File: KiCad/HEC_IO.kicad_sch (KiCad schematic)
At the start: 23 parts, among them SW1 SW_DIP_x04, U12 74LS04, U17 74LS20, U22 74LS02, U30 74LS74, U31 74LS32, U32 LM79M05_TO220, U33 74LS20, U34 74LS393, U35 74LS08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

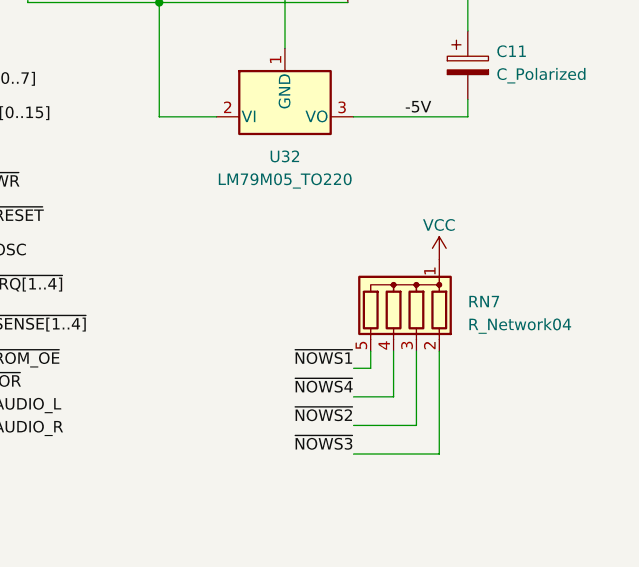
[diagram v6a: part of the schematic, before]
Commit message: Change resistor network, add revision number
Changed most of the resistor network footprints so that they would accept both 9 pin and 5 pin resistor networks (since I bought 50 of those 5 pin ones!). Power routing optimizations. Added a revision number to the silkscreen to distinguish the board
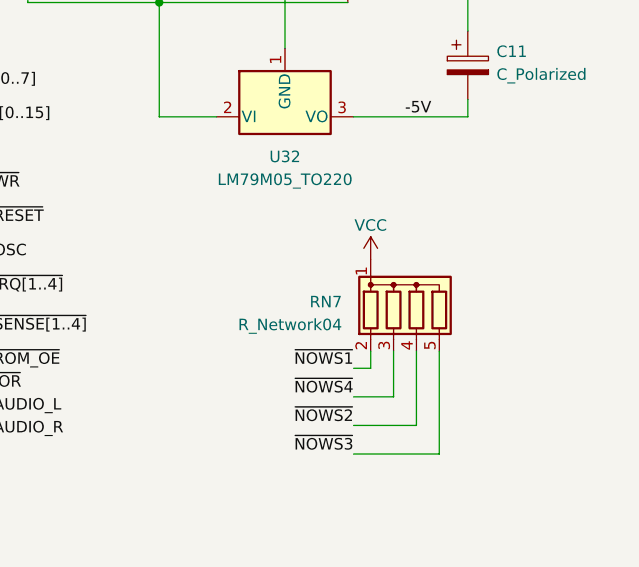
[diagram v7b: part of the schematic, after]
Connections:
- net ~{NOWS1}: now also RN7.2 (R1); no longer RN7.5 (R4)
- net ~{NOWS2}: now also RN7.4 (R3); no longer RN7.3 (R2)
- net ~{NOWS3}: now also RN7.5 (R4); no longer RN7.2 (R1)
- net ~{NOWS4}: now also RN7.3 (R2); no longer RN7.4 (R3)
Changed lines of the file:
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@@
     )
   )
-  (symbol (lib_id "Device:R_Network04") (at 260.35 66.04 0) (mirror y) (unit 1)
-    (in_bom yes) (on_board yes) (dnp no) (fields_autoplaced)
-    (property "Reference" "RN7" (at 268.605 65.659 0)
+  (symbol (lib_id "Device:R_Network04") (at 262.89 66.04 0) (unit 1)
+    (in_bom yes) (on_board yes) (dnp no)
+    (property "Reference" "RN7" (at 254.635 65.659 0)
       (effects (font (size 1.27 1.27)) (justify right))
     )
-    (property "Value" "R_Network04" (at 268.605 68.199 0)
+    (property "Value" "R_Network04" (at 254.635 68.199 0)
       (effects (font (size 1.27 1.27)) (justify right))
     )
-    (property "Footprint" "Resistor_THT:R_Array_SIP5" (at 253.365 66.04 90)
-      (effects (font (size 1.27 1.27)) hide)
-    )
-    (property "Datasheet" "http://www.vishay.com/docs/31509/csc.pdf" (at 260.35 66.04 0)
+    (property "Footprint" "Resistor_THT:R_Array_SIP5" (at 269.875 66.04 90)
+      (effects (font (size 1.27 1.27)) hide)
+    )
+    (property "Datasheet" "http://www.vishay.com/docs/31509/csc.pdf" (at 262.89 66.04 0)
       (effects (font (size 1.27 1.27)) hide)
     )
@@
     )
   )
-  (symbol (lib_id "power:VCC") (at 265.43 60.96 0) (unit 1)
-    (in_bom yes) (on_board yes) (dnp no) (fields_autoplaced)
-    (property "Reference" "#PWR0130" (at 265.43 64.77 0)
-      (effects (font (size 1.27 1.27)) hide)
-    )
-    (property "Value" "VCC" (at 265.43 57.15 0)
-      (effects (font (size 1.27 1.27)))
-    )
-    (property "Footprint" "" (at 265.43 60.96 0)
-      (effects (font (size 1.27 1.27)) hide)
-    )
-    (property "Datasheet" "" (at 265.43 60.96 0)
-      (effects (font (size 1.27 1.27)) hide)
-    )
+  (symbol (lib_id "power:VCC") (at 257.81 60.96 0) (unit 1)
+    (in_bom yes) (on_board yes) (dnp no) (fields_autoplaced)
+    (property "Reference" "#PWR0130" (at 257.81 64.77 0)
+      (effects (font (size 1.27 1.27)) hide)
+    )
+    (property "Value" "VCC" (at 257.81 57.15 0)
+      (effects (font (size 1.27 1.27)))
+    )
+    (property "Footprint" "" (at 257.81 60.96 0)
+      (effects (font (size 1.27 1.27)) hide)
+    )
+    (property "Datasheet" "" (at 257.81 60.96 0)
+      (effects (font (size 1.27 1.27)) hide)
+    )

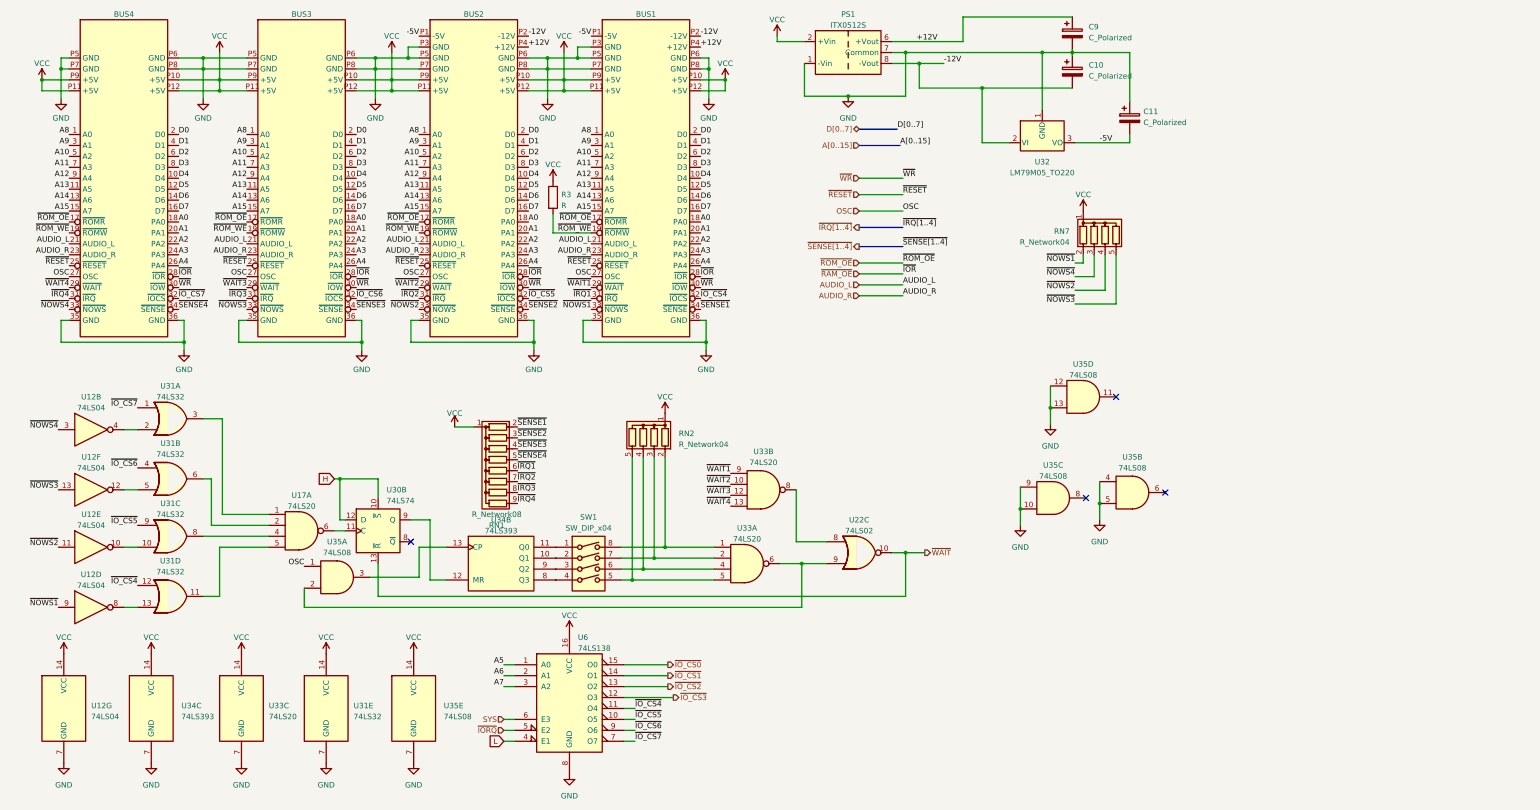
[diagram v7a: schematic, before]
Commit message: Add I2C bus
Change audio pins on the bus to carry I2C signal. This can be used for configuring onboard devices such as RGB to HDMI converters, sound mixers, GPIOs, etc.
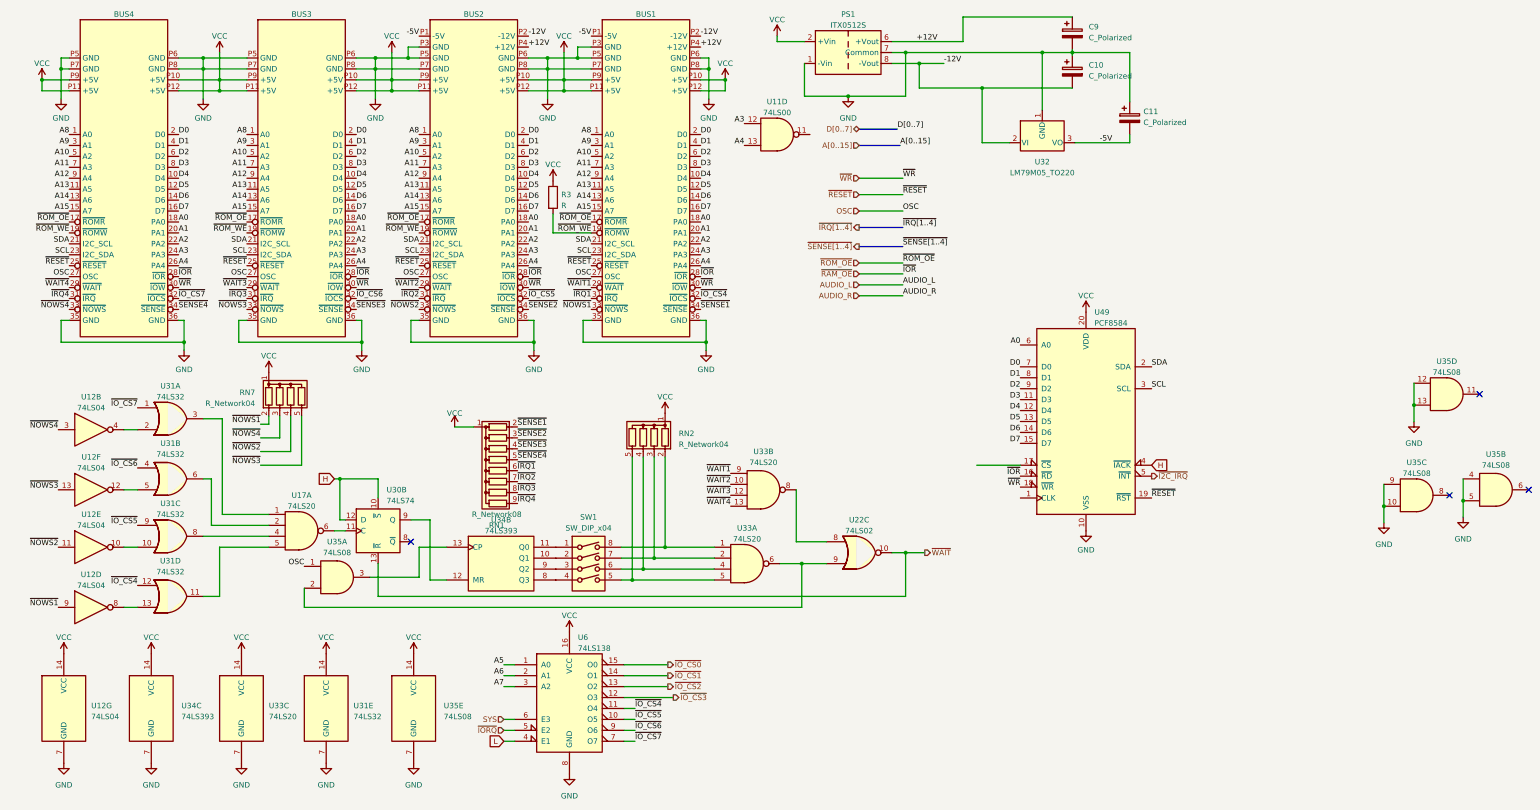
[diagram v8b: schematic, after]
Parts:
- added U11: 74LS00, Library:DIP-14_W7.62mm_Socket_ThinPads, symbol 74xx:74LS00
- added U49: PCF8584, symbol Interface_Expansion:PCF8584
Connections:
- net A0: now also U49.6 (A0)
- net A3: now also U11.12
- net A4: now also U11.13
- net AUDIO_L: no longer BUS1.21 (AUDIO_L), BUS2.21 (AUDIO_L), BUS3.21 (AUDIO_L), BUS4.21 (AUDIO_L)
- net AUDIO_R: no longer BUS1.23 (AUDIO_R), BUS2.23 (AUDIO_R), BUS3.23 (AUDIO_R), BUS4.23 (AUDIO_R)
- net D0: now also U49.7 (D0)
- net D1: now also U49.8 (D1)
- net D2: now also U49.9 (D2)
- net D3: now also U49.11 (D3)
- net D4: now also U49.12 (D4)
- net D5: now also U49.13 (D5)
- net D6: now also U49.14 (D6)
- net D7: now also U49.15 (D7)
- net GND: now also U49.10 (VSS)
- net H: now also U49.4 (~{IACK})
- net VCC: now also U49.20 (VDD)
- net ~{RAM_OE}: now also U49.16 (~{RD})
- net ~{RESET}: now also U49.19 (~{RST})
- net ~{WR}: now also U49.18 (~{WR})
- new net SCL: BUS1.23 (I2C_SDA), BUS2.23 (I2C_SDA), BUS3.23 (I2C_SDA), BUS4.23 (I2C_SDA), U49.3 (SCL)
- new net SDA: BUS1.21 (I2C_SCL), BUS2.21 (I2C_SCL), BUS3.21 (I2C_SCL), BUS4.21 (I2C_SCL), U49.2 (SDA)
- new net ~{I2C_IRQ}: U49.5 (~{INT})
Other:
- moved on the sheet: RN7, U35B, U35C, U35D
